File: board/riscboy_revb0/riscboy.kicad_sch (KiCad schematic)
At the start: 104 parts, among them J1 USB_B_Micro, J10 NF, J2 NF, J3 1827928-1 TE, J4 2.54mm, J5 2.54mm, J6 2.54mm, J7 2.54mm, J8 2.5mm-3P-TRS, J9 0.5mm FFC bottom-contact, SW1 membrane, SW10 tactile, SW2 membrane, SW3 membrane, SW4 membrane, SW5 SW_SPDT, SW6 membrane, SW7 membrane, SW8 membrane, SW9 membrane, U1 RP2040, U10 iCE40-HX8k-BG121, U11 W25Q16JV, U2 MIC23050-4YML, U3 W25Q16JV, U4 MCP73831-SOT-23-5, U5 MIC23050-SYML, U6 74LVC2G04, U7 NCP115ASN330, U8 74LVC2G04, U9 CY7C1041CV33, Y1 12M

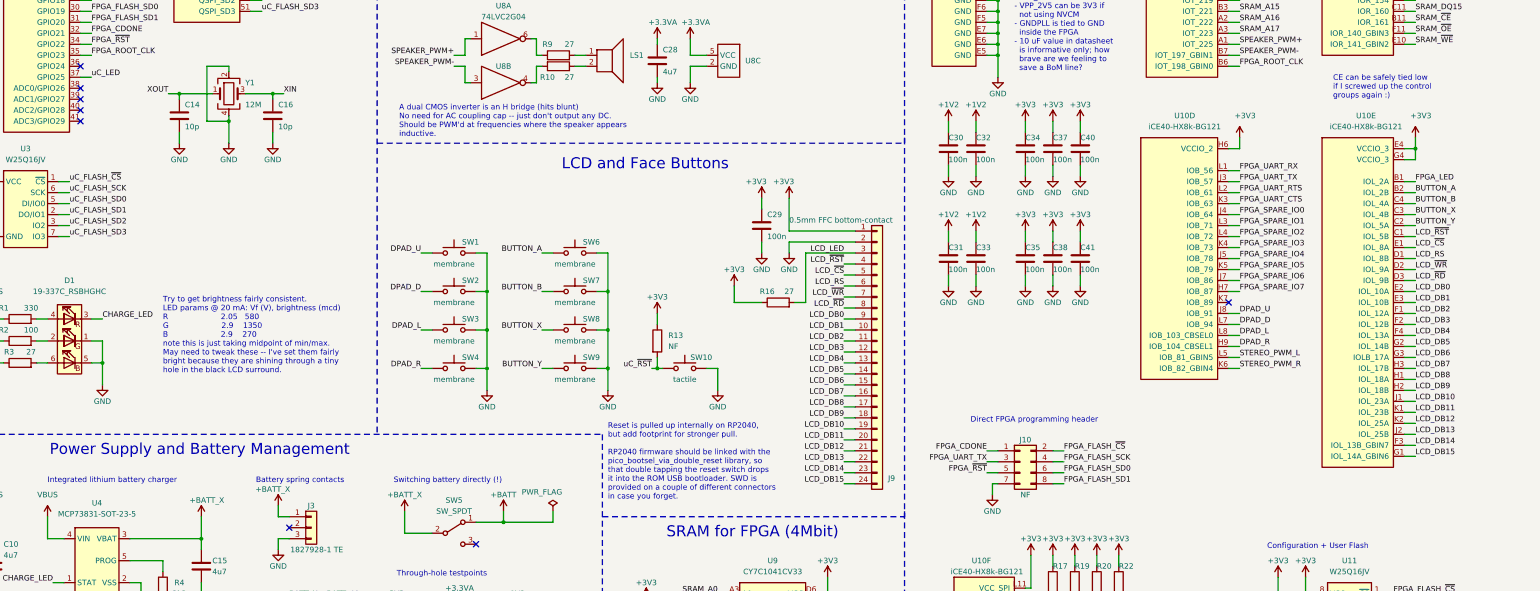
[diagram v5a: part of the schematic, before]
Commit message: Add missing start/select buttons, and move LCD reset control to uC to make room for FPGA IOs.
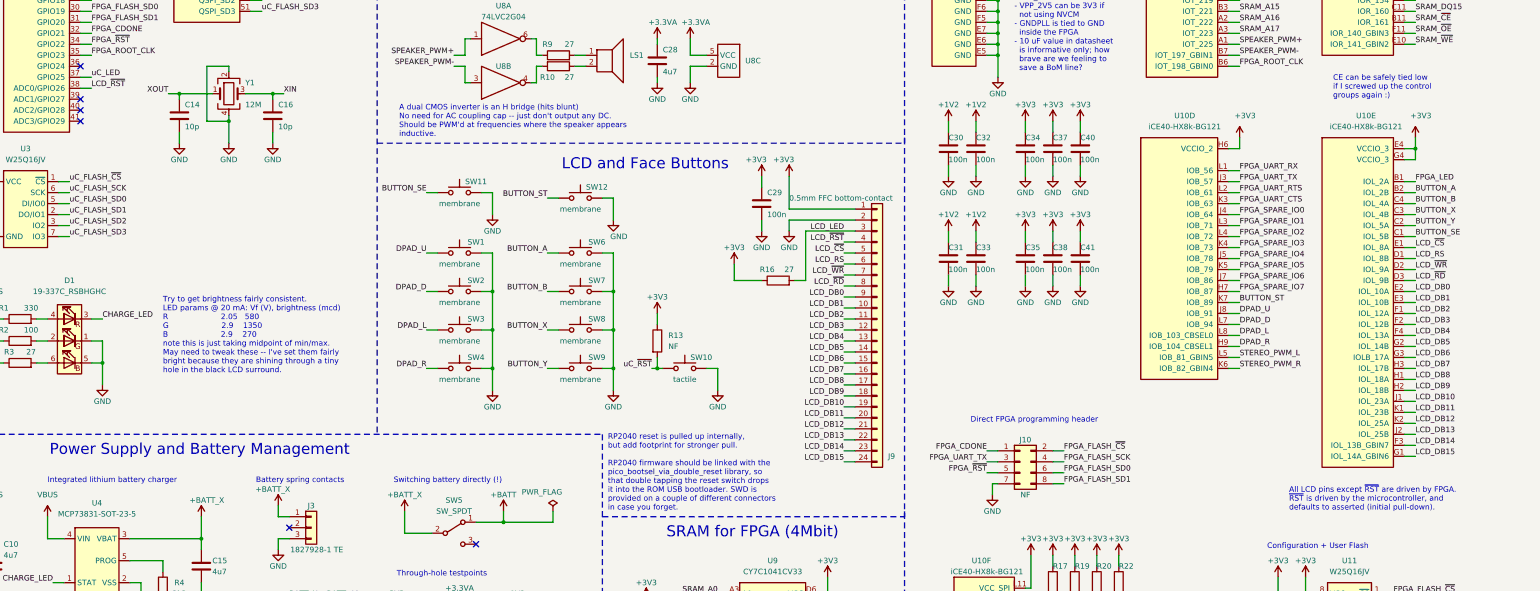
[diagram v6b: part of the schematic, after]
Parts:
- added SW11, SW12: membrane, riscboy:membrane-switch-6mm, symbol Switch:SW_Push
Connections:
- net GND: now also SW11.2, SW12.2
- net LCD_~RST~: now also U1.38 (ADC0/GPIO26); no longer U10.C1 (IOL_5B)
- net BUTTON_ST: now reaches U10.K7 (IOB_89)
- net BUTTON_ST: now also SW12.1
- new net BUTTON_SE: SW11.1, U10.C1 (IOL_5B)
- no-connect marks 14 -> 12
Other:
- note added: "All LCD pins except ~RST~ are driven by FPGA. ~RST~ is driven by the microcontroller, and defaults to asserted (initial pull-down)."
- note added: "RP2040 reset is pulled up internally, but add footprint for stronger pull. RP2040 firmware should be linked with the pico_bootsel_via_double_reset library, so that double tapping the reset switch drops it into the ROM USB bootloader. SWD is provided on a couple of different connectors in case you forget."
- note removed: "Reset is pulled up internally on RP2040, but add footprint for stronger pull. RP2040 firmware should be linked with the pico_bootsel_via_double_reset library, so that double tapping the reset switch drops it into the ROM USB bootloader. SWD is provided on a couple of different connectors in case you forget."
- moved on the sheet: C29, J9, R16, SW1, SW2, SW3, SW4, SW6, SW7, SW8, SW9
